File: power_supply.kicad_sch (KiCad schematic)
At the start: 19 parts, among them J7 12V AC, U1 MC78M12_TO252, U2 MC79M12_TO252, U3 L78L05_SO8, U4 L79L05_SO8

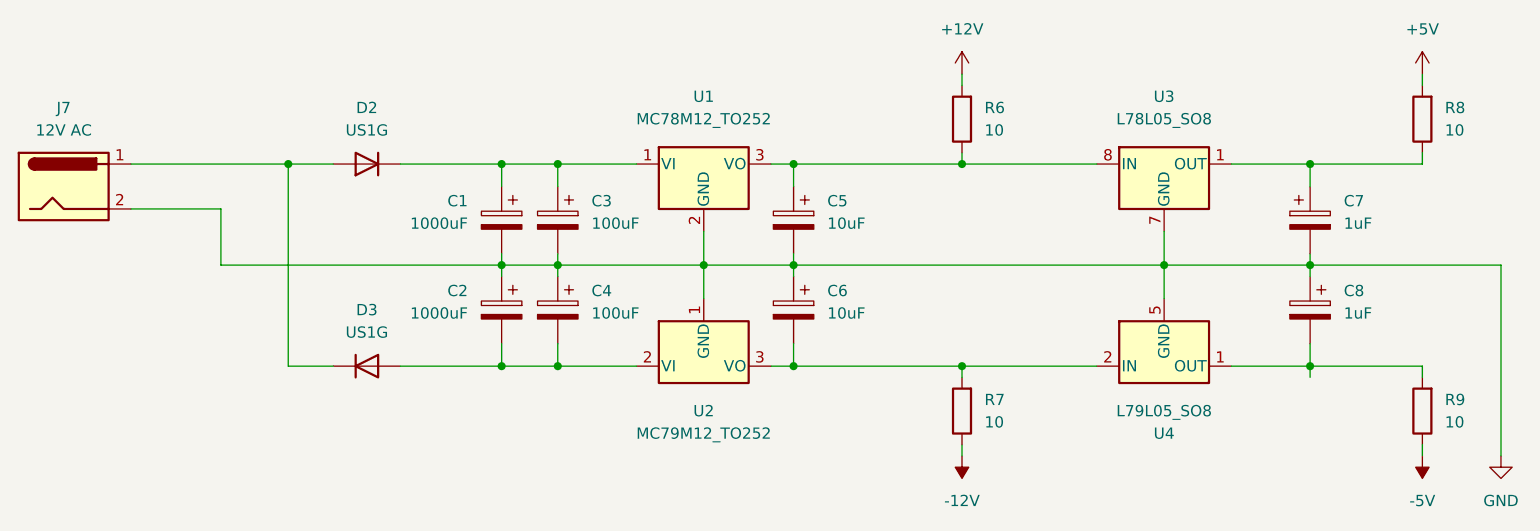
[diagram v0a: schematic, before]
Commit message: Fix power supply, add schematics pdf
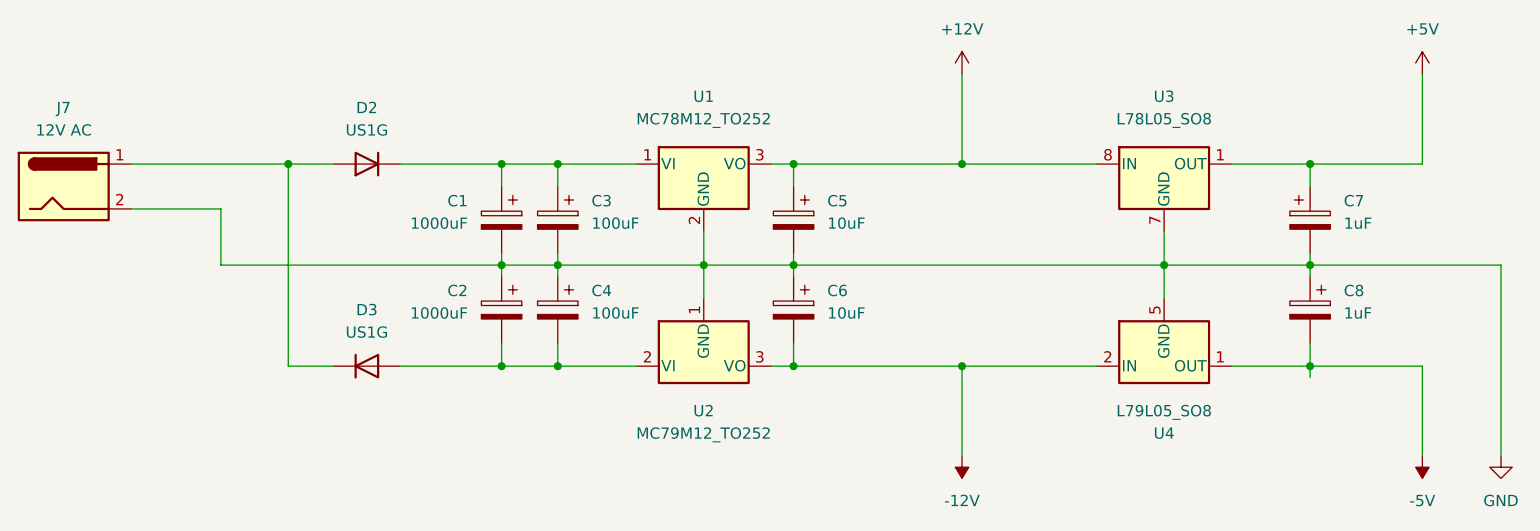
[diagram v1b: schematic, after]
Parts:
- removed R6, R7, R8, R9: 10, Resistor_SMD:R_1206_3216Metric_Pad1.30x1.75mm_HandSolder, symbol Device:R
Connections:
- net +12V: now also C5.1, U1.3 (VO), U3.8 (IN)
- net +5V: now also C7.1, U3.1 (OUT)
- net -12V: now also C6.2, U2.3 (VO), U4.2 (IN), U4.3 (IN), U4.6 (IN), U4.7 (IN)
- net -5V: now also C8.2, U4.1 (OUT)
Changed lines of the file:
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@@
-    (stroke (width 0) (type default) (color 0 0 0 0))
-  )
-  (wire (pts (xy 146.05 74.93) (xy 146.05 76.2))
     (stroke (width 0) (type default) (color 0 0 0 0))
   )
@@
     (stroke (width 0) (type default) (color 0 0 0 0))
   )
-  (wire (pts (xy 146.05 107.95) (xy 146.05 109.22))
-    (stroke (width 0) (type default) (color 0 0 0 0))
-  )
   (wire (pts (xy 93.98 96.52) (xy 93.98 97.79))
     (stroke (width 0) (type default) (color 0 0 0 0))
   )
-  (wire (pts (xy 146.05 83.82) (xy 146.05 85.09))
+  (wire (pts (xy 146.05 74.93) (xy 146.05 85.09))
     (stroke (width 0) (type default) (color 0 0 0 0))
   )
@@
     (stroke (width 0) (type default) (color 0 0 0 0))
   )
-  (wire (pts (xy 198.12 107.95) (xy 198.12 109.22))
-    (stroke (width 0) (type default) (color 0 0 0 0))
-  )
-  (wire (pts (xy 146.05 116.84) (xy 146.05 118.11))
+  (wire (pts (xy 146.05 107.95) (xy 146.05 118.11))
     (stroke (width 0) (type default) (color 0 0 0 0))
   )
@@
     (stroke (width 0) (type default) (color 0 0 0 0))
   )
-  (wire (pts (xy 198.12 83.82) (xy 198.12 85.09))
-    (stroke (width 0) (type default) (color 0 0 0 0))
-  )
   (wire (pts (xy 82.55 107.95) (xy 93.98 107.95))
     (stroke (width 0) (type default) (color 0 0 0 0))
@@
     (stroke (width 0) (type default) (color 0 0 0 0))
   )
-  (wire (pts (xy 198.12 116.84) (xy 198.12 118.11))
+  (wire (pts (xy 198.12 107.95) (xy 198.12 118.11))
     (stroke (width 0) (type default) (color 0 0 0 0))
   )
@@
     (stroke (width 0) (type default) (color 0 0 0 0))
   )
-  (wire (pts (xy 198.12 74.93) (xy 198.12 76.2))
+  (wire (pts (xy 198.12 74.93) (xy 198.12 85.09))
     (stroke (width 0) (type default) (color 0 0 0 0))
   )
@@
     (pin "2")
   )
-  (symbol (lib_id "Device:R") (at 146.05 113.03 180) (unit 1)
-    (in_bom yes) (on_board yes) (fields_autoplaced)
-    (property "Reference" "R7" (id 0) (at 148.59 111.7599 0)
-      (effects (font (size 1.27 1.27)) (justify right))
-    )
-    (property "Value" "10" (id 1) (at 148.59 114.2999 0)
-      (effects (font (size 1.27 1.27)) (justify right))
-    )
-    (property "Footprint" "Resistor_SMD:R_1206_3216Metric_Pad1.30x1.75mm_HandSolder" (id 2) (at 147.828 113.03 90)
-      (effects (font (size 1.27 1.27)) hide)
-    )
-    (property "Datasheet" "~" (id 3) (at 146.05 113.03 0)
-      (effects (font (size 1.27 1.27)) hide)
-    )
-    (property "LCSC" "C17902" (id 4) (at 146.05 113.03 0)
-      (effects (font (size 1.27 1.27)) hide)
-    )
-    (pin "1")
-    (pin "2")
-  )
   (symbol (lib_id "Device:C_Polarized") (at 93.98 91.44 0) (mirror y) (unit 1)
     (in_bom yes) (on_board yes) (fields_autoplaced)
@@
     (pin "1")
   )
-  (symbol (lib_id "Device:R") (at 198.12 80.01 180) (unit 1)
-    (in_bom yes) (on_board yes) (fields_autoplaced)
-    (property "Reference" "R8" (id 0) (at 200.66 78.7399 0)
-      (effects (font (size 1.27 1.27)) (justify right))
-    )
-    (property "Value" "10" (id 1) (at 200.66 81.2799 0)
-      (effects (font (size 1.27 1.27)) (justify right))
-    )
-    (property "Footprint" "Resistor_SMD:R_1206_3216Metric_Pad1.30x1.75mm_HandSolder" (id 2) (at 199.898 80.01 90)
-      (effects (font (size 1.27 1.27)) hide)
-    )
-    (property "Datasheet" "~" (id 3) (at 198.12 80.01 0)
-      (effects (font (size 1.27 1.27)) hide)
-    )
-    (property "LCSC" "C17902" (id 4) (at 198.12 80.01 0)
-      (effects (font (size 1.27 1.27)) hide)
-    )
-    (pin "1")
-    (pin "2")
-  )
   (symbol (lib_id "Regulator_Linear:MC79M12_TO252") (at 116.84 107.95 0) (unit 1)
     (in_bom yes) (on_board yes) (fields_autoplaced)
@@
     (pin "1")
   )
-  (symbol (lib_id "Device:R") (at 198.12 113.03 180) (unit 1)
-    (in_bom yes) (on_board yes) (fields_autoplaced)
-    (property "Reference" "R9" (id 0) (at 200.66 111.7599 0)
-      (effects (font (size 1.27 1.27)) (justify right))
-    )
-    (property "Value" "10" (id 1) (at 200.66 114.2999 0)
-      (effects (font (size 1.27 1.27)) (justify right))
-    )
-    (property "Footprint" "Resistor_SMD:R_1206_3216Metric_Pad1.30x1.75mm_HandSolder" (id 2) (at 199.898 113.03 90)
-      (effects (font (size 1.27 1.27)) hide)
-    )
-    (property "Datasheet" "~" (id 3) (at 198.12 113.03 0)
-      (effects (font (size 1.27 1.27)) hide)
-    )
-    (property "LCSC" "C17902" (id 4) (at 198.12 113.03 0)
-      (effects (font (size 1.27 1.27)) hide)
-    )
-    (pin "1")
-    (pin "2")
-  )
   (symbol (lib_id "Diode:US1G") (at 78.74 85.09 180) (unit 1)
     (in_bom yes) (on_board yes) (fields_autoplaced)
@@
       (effects (font (size 1.27 1.27)) hide)
     )
-    (pin "1")
-    (pin "2")
-  )
-  (symbol (lib_id "Device:R") (at 146.05 80.01 180) (unit 1)
-    (in_bom yes) (on_board yes) (fields_autoplaced)
-    (property "Reference" "R6" (id 0) (at 148.59 78.7399 0)
-      (effects (font (size 1.27 1.27)) (justify right))
-    )
-    (property "Value" "10" (id 1) (at 148.59 81.2799 0)
-      (effects (font (size 1.27 1.27)) (justify right))
-    )
-    (property "Footprint" "Resistor_SMD:R_1206_3216Metric_Pad1.30x1.75mm_HandSolder" (id 2) (at 147.828 80.01 90)
-      (effects (font (size 1.27 1.27)) hide)
-    )
-    (property "Datasheet" "~" (id 3) (at 146.05 80.01 0)
-      (effects (font (size 1.27 1.27)) hide)
-    )
-    (property "LCSC" "C17902" (id 4) (at 146.05 80.01 0)
-      (effects (font (size 1.27 1.27)) hide)
-    )
